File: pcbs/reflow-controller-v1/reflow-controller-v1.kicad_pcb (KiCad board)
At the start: 4 copper layers, 85.2 x 238.5 mm, 154 parts, among them J1 PinHeader 1x03 P2.54mm, J101 EB163A-03-C-180, J102 EB163A-02-C-180, J103 EB163A-02-C-180, J104 EB163A-02-C-180, J105 EB163A-02-C-180, J106 PinHeader 1x03 P2.54mm, J1101 EB163A-04-C-180, J1201 EB163A-04-C-180, J1301 EB163A-04-C-180, J201 PinHeader 1x02 P2.54mm, J3 SWD, J4 UART, M101 47053-1000, Q1601 MMBT3904, Q1602 140357145200, Q201 PMV65XP, SW1001 TS04-66-85-BK-160-SMT, SW1002 PEC12R-3220F-S0024, SW1003 TS04-66-85-BK-160-SMT, U1 TMP1075DSG, U1101 MAX31865ATP+, U1201 MAX31865ATP+, U1301 MAX31865ATP+, U2 TMP1075DSG, U201 TPS62933DRLR, U202 AZ1117-3.3, U3 STM32G474VETx, U301 MOC3043SM, U401 MOC3043SM, U501 MOC3043SM, U601 MOC3043SM

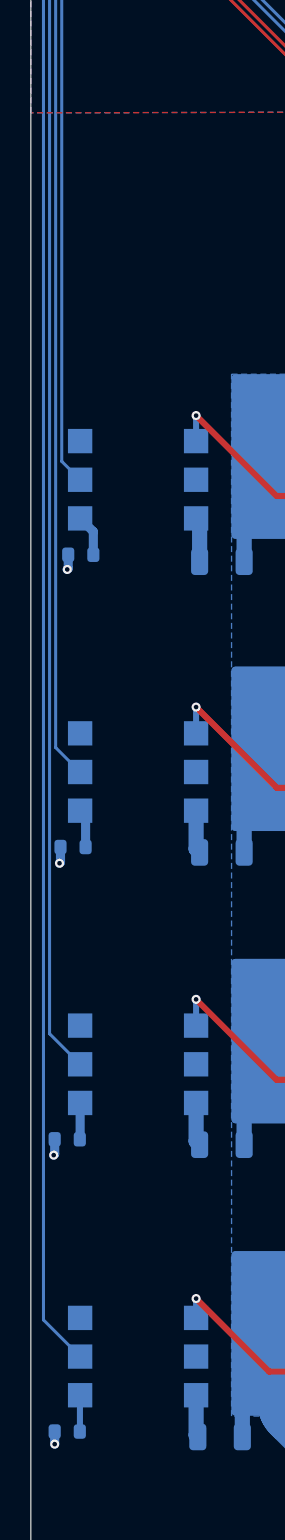
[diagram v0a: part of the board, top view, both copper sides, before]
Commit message: improve powerdelivery to optotriacs
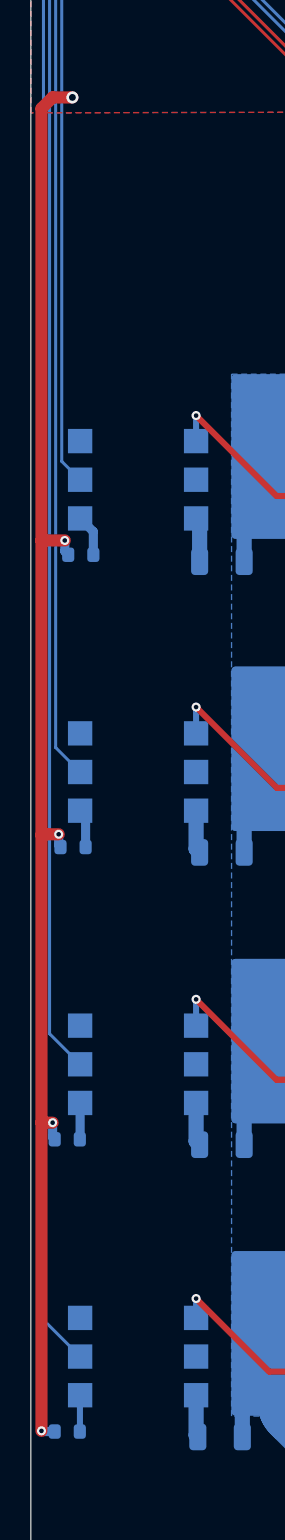
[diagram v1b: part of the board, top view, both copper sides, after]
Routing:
- net +3V3: track 98.0 -> 190.6 mm, vias 32 -> 33
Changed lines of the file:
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@@
 	)
 	(segment
+		(start 17.8308 144.3736)
+		(end 19.134 144.3736)
+		(width 0.8)
+		(layer "F.Cu")
+		(net 2)
+	)
+	(segment
+		(start 17.1026 145.1018)
+		(end 17.8308 144.3736)
+		(width 0.8)
+		(layer "F.Cu")
+		(net 2)
+	)
+	(segment
+		(start 17.1026 192.8368)
+		(end 17.1026 173.482)
+		(width 0.8)
+		(layer "F.Cu")
+		(net 2)
+	)
+	(segment
 		(start 87.2046 85.9692)
 		(end 73.1456 85.9692)
@@
 		(net 2)
 	)
+	(segment
+		(start 17.834 211.7344)
+		(end 17.1026 211.7344)
+		(width 0.8)
+		(layer "F.Cu")
+		(net 2)
+	)
+	(segment
+		(start 17.1026 231.9856)
+		(end 17.1026 211.7344)
+		(width 0.8)
+		(layer "F.Cu")
+		(net 2)
+	)
+	(segment
+		(start 17.1026 173.482)
+		(end 17.1026 145.1018)
+		(width 0.8)
+		(layer "F.Cu")
+		(net 2)
+	)
+	(segment
+		(start 18.234 192.786)
+		(end 17.1534 192.786)
+		(width 0.8)
+		(layer "F.Cu")
+		(net 2)
+	)
+	(segment
+		(start 17.1534 192.786)
+		(end 17.1026 192.8368)
+		(width 0.8)
+		(layer "F.Cu")
+		(net 2)
+	)
+	(segment
+		(start 17.1026 211.7344)
+		(end 17.1026 192.8368)
+		(width 0.8)
+		(layer "F.Cu")
+		(net 2)
+	)
+	(segment
+		(start 18.634 173.482)
+		(end 17.1026 173.482)
+		(width 0.8)
+		(layer "F.Cu")
+		(net 2)
+	)
 	(via
 		(at 54.102 144.78)
@@
 	)
 	(via
-		(at 17.971 232.854)
+		(at 17.1026 231.9856)
 		(size 0.6)
 		(drill 0.3)
@@
 	)
 	(via
-		(at 18.288 194.691)
+		(at 18.234 192.786)
 		(size 0.6)
 		(drill 0.3)
@@
 	)
 	(via
-		(at 17.907 213.868)
+		(at 17.834 211.7344)
 		(size 0.6)
 		(drill 0.3)
@@
 	)
 	(via
-		(at 18.796 175.387)
+		(at 18.634 173.482)
 		(size 0.6)
 		(drill 0.3)
@@
 	)
 	(via
+		(at 19.134 144.3736)
+		(size 0.8)
+		(drill 0.45)
+		(layers "F.Cu" "B.Cu")
+		(free yes)
+		(net 2)
+	)
+	(via
 		(at 49.4792 74.1934)
 		(size 0.6)
@@
 	)
 	(segment
+		(start 18.634 174.1958)
+		(end 18.86 174.4218)
+		(width 0.6)
+		(layer "B.Cu")
+		(net 2)
+	)
+	(segment
 		(start 54.102 152.576)
 		(end 54.102 144.78)
@@
 	)
 	(segment
-		(start 18.352 194.627)
-		(end 18.288 194.691)
-		(width 0.6)
-		(layer "B.Cu")
-		(net 2)
-	)
-	(segment
 		(start 70.4088 88.5444)
 		(end 70.5704 88.5444)
@@
 	)
 	(segment
-		(start 18.86 175.323)
-		(end 18.796 175.387)
-		(width 0.6)
-		(layer "B.Cu")
-		(net 2)
-	)
-	(segment
 		(start 74.9282 108.9232)
 		(end 74.9282 110.3988)
@@
 	)
 	(segment
+		(start 17.1026 231.9856)
+		(end 17.146 232.029)
+		(width 0.6)
+		(layer "B.Cu")
+		(net 2)
+	)
+	(segment
 		(start 28.9182 70.9298)
 		(end 28.9052 70.9168)
@@
 	)
 	(segment
+		(start 17.146 232.029)
+		(end 17.971 232.029)
+		(width 0.6)
+		(layer "B.Cu")
+		(net 2)
+	)
+	(segment
 		(start 76.9112 89.4662)
 		(end 74.5744 89.4662)
@@
 	)
 	(segment
-		(start 17.971 212.8266)
-		(end 17.971 213.804)
+		(start 17.834 212.6896)
+		(end 17.971 212.8266)
 		(width 0.6)
 		(layer "B.Cu")
@@
 	)
 	(segment
-		(start 18.86 174.4218)
-		(end 18.86 175.323)
-		(width 0.6)
-		(layer "B.Cu")
-		(net 2)
-	)
-	(segment
 		(start 31.585 76.811)
 		(end 29.525 76.811)
@@
 	)
 	(segment
+		(start 18.234 193.5062)
+		(end 18.352 193.6242)
+		(width 0.6)
+		(layer "B.Cu")
+		(net 2)
+	)
+	(segment
 		(start 44.982 91.9895)
 		(end 44.982 92.813)
@@
 	)
 	(segment
-		(start 17.971 232.854)
-		(end 17.971 232.029)
-		(width 0.6)
-		(layer "B.Cu")
-		(net 2)
-	)
-	(segment
 		(start 82.369 58.5816)
 		(end 82.55 58.7626)
@@
 	)
 	(segment
-		(start 17.971 213.804)
-		(end 17.907 213.868)
-		(width 0.6)
-		(layer "B.Cu")
-		(net 2)
-	)
-	(segment
 		(start 75.375 111.4552)
 		(end 76.2386 112.3188)
@@
 	)
 	(segment
-		(start 18.352 193.6242)
-		(end 18.352 194.627)
+		(start 18.234 192.786)
+		(end 18.234 193.5062)
+		(width 0.6)
+		(layer "B.Cu")
+		(net 2)
+	)
+	(segment
+		(start 18.634 173.482)
+		(end 18.634 174.1958)
 		(width 0.6)
 		(layer "B.Cu")
@@
 	)
 	(segment
+		(start 17.834 211.7344)
+		(end 17.834 212.6896)
+		(width 0.6)
+		(layer "B.Cu")
+		(net 2)
+	)
+	(segment
 		(start 75.375 110.8456)
 		(end 75.375 111.4552)
@@
 		(polygon
 			(pts
-				(xy 16.383 15.24) (xy 101.5238 15.24) (xy 101.5746 159.6644) (xy 64.516 159.7152) (xy 64.516015 145.209658)
-				(xy 20.49774 145.237321) (xy 20.5486 233.299) (xy 16.4084 233.2736)
+				(xy 16.383 15.24) (xy 101.5238 15.24) (xy 101.5746 159.6644) (xy 64.516 159.7152) (xy 64.516015 145.288)
+				(xy 16.4084 145.3896)
 			)
 		)

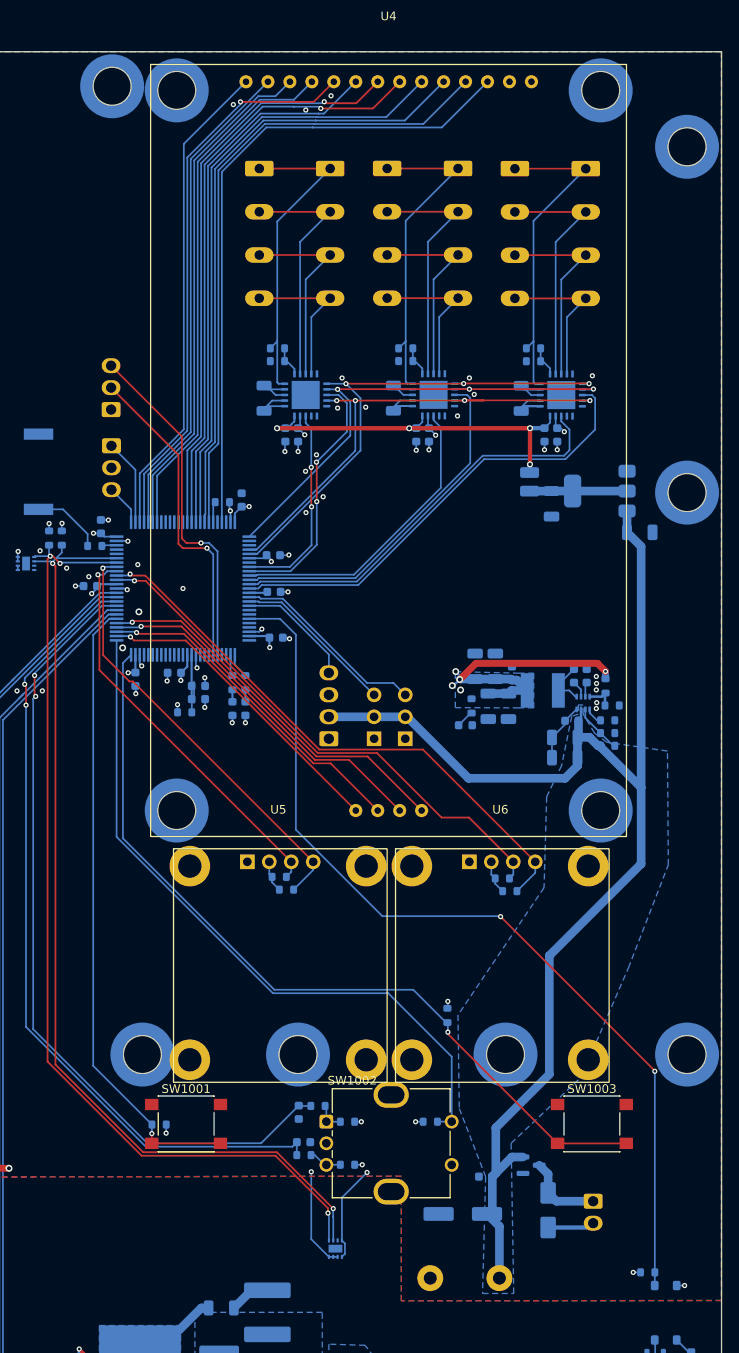
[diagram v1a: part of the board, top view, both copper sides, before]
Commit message: add clear border between HV&LV
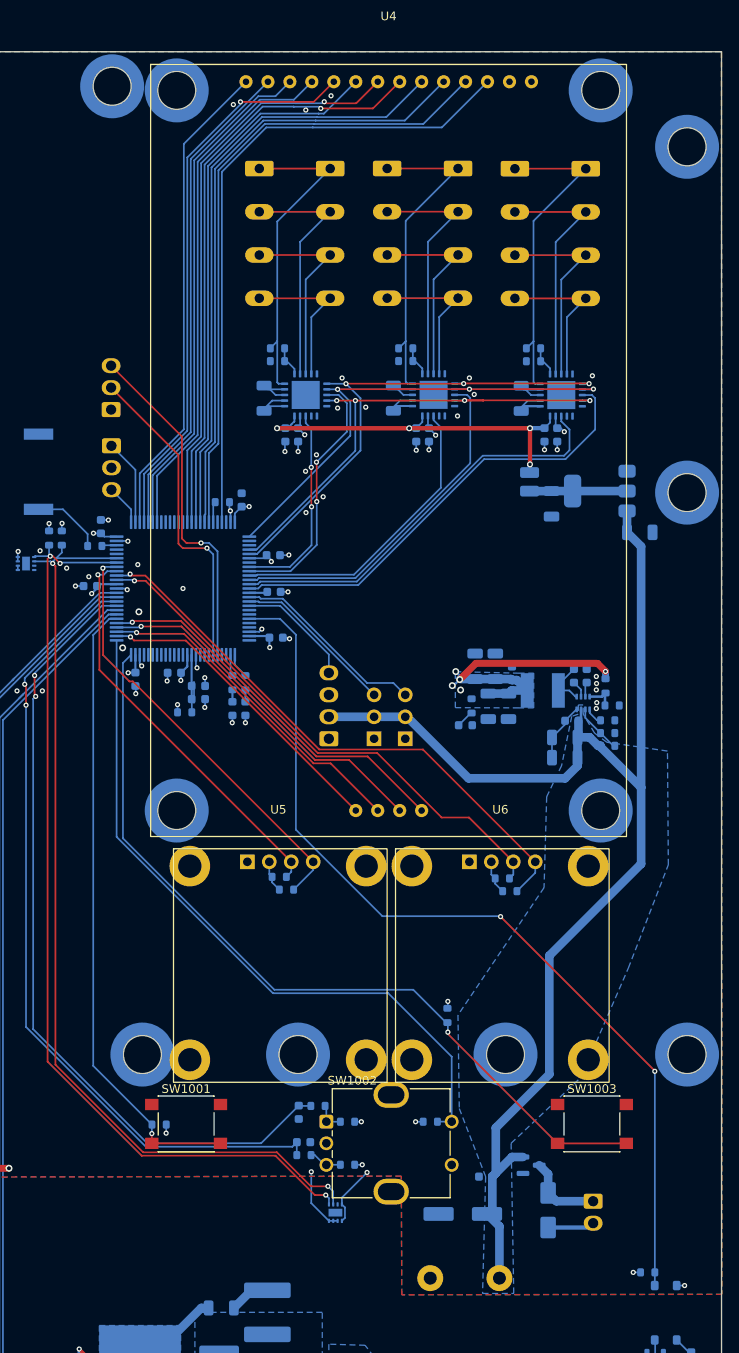
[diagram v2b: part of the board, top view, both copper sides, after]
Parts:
- moved U2 4.17 mm to (56.9, 149.5)
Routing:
- net +3V3: track 190.6 -> 186.4 mm
- net GND: track 48.7 -> 44.5 mm
- net /Temperature onboard 1/SDA: track 113.1 -> 109.7 mm
- net /Temperature onboard 1/SCL: track 112.8 -> 109.8 mm

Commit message: update pcb size&display positioning
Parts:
- moved R2 119.2 mm to (120.8, 142.7), turned to 180 degrees
- moved R1 118.9 mm to (120.8, 140.2), turned to 180 degrees
- moved U1 116.3 mm to (116.6, 140.8)
- moved Q1602 99.2 mm to (31.9, 237.5), turned to 180 degrees
- moved R1603 93.9 mm to (37.2, 237.9), turned to 0 degrees
- moved R1605 92.9 mm to (59.8, 69.7), turned to 90 degrees
- moved Q1601 92.9 mm to (37.5, 240.7)
- moved D1601 92.2 mm to (42.4, 250.8)
- moved D1603 92.2 mm to (37.7, 250.8)
- moved D1604 92.2 mm to (40.1, 250.8)
- moved R1604 92.2 mm to (38.1, 247.8)
- moved D1602 92.2 mm to (41.1, 254.2)
- moved D1605 92.0 mm to (38.1, 244.9)
- moved C1602 90.9 mm to (41.6, 243.7), turned to -90 degrees
- moved R1601 80.6 mm to (45.2, 240.8), turned to -90 degrees
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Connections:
- J4 pad 2: /microcontroller/USART1_RX -> /microcontroller/USART2_RX
- J4 pad 3: /microcontroller/USART1_TX -> /microcontroller/USART2_TX
- U3 pad 15: /Servo1 -> unconnected-(U3-PC0-Pad15)
- U3 pad 16: /Servo2 -> unconnected-(U3-PC1-Pad16)
- U3 pad 17: /Fan_PWM -> unconnected-(U3-PC2-Pad17)
- U3 pad 30: /microcontroller/USART1_TX -> unconnected-(U3-PC4-Pad30)
- U3 pad 31: /microcontroller/USART1_RX -> unconnected-(U3-PC5-Pad31)
- U3 pad 39: unconnected-(U3-PE8-Pad39) -> /Servo1
- U3 pad 40: unconnected-(U3-PE9-Pad40) -> /Servo2
- U3 pad 42: unconnected-(U3-PE11-Pad42) -> /Fan_PWM
- U3 pad 87: unconnected-(U3-PD5-Pad87) -> /microcontroller/USART2_TX
- U3 pad 88: unconnected-(U3-PD6-Pad88) -> /microcontroller/USART2_RX
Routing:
- net /Temperature onboard 1/SCL: track 109.8 -> 0.00 mm, vias 2 -> 0
- net /Temperature onboard 1/SDA: track 109.7 -> 0.00 mm, vias 3 -> 0
- net +3V3: track 186.4 -> 80.7 mm, vias 33 -> 23
- net /Phase_L: track 111.9 -> 28.2 mm, vias 16 -> 12
- net /Buttons/SW_Encoder: track 81.2 -> 0.00 mm
- net /Zero Crossing detector/Crossing: track 106.6 -> 182.8 mm
- net /Buttons/SW_2: track 95.2 -> 27.2 mm
- net /Buttons/SW_1: track 73.1 -> 10.1 mm
- net /Display OLED 2/I2C_SDA: track 66.6 -> 4.57 mm, vias 1 -> 0
- net /Display OLED 2/I2C_SCL: track 61.5 -> 5.88 mm
- net /Buttons/Encoder_A: track 93.5 -> 39.5 mm, vias 2 -> 1
- net /Buttons/Encoder_B: track 93.5 -> 43.2 mm, vias 2 -> 1
- net /microcontroller/USART1_TX: track 40.1 -> 0.00 mm, vias 1 -> 0
- net /microcontroller/USART1_RX: track 37.4 -> 0.00 mm, vias 1 -> 0
- net /Display LCD/Touch: track 44.5 -> 18.0 mm
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- removed copper zone on F.Cu, net /Phase_L
- removed copper zone on B.Cu, net /Phase_N
- removed copper zone on B.Cu, net /SSR 1/MAIN_OUT
- removed copper zone on B.Cu, net /SSR 2/MAIN_OUT
- removed copper zone on B.Cu, net /SSR 3/MAIN_OUT
- removed copper zone on B.Cu, net /SSR 4/MAIN_OUT
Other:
- board size 85.2 x 238.5 mm -> 74.9 x 243.5 mm
- board text added: "Fix it"
- board text added: "Standofs NEED to be at least 23mm to clear the DCDC module"

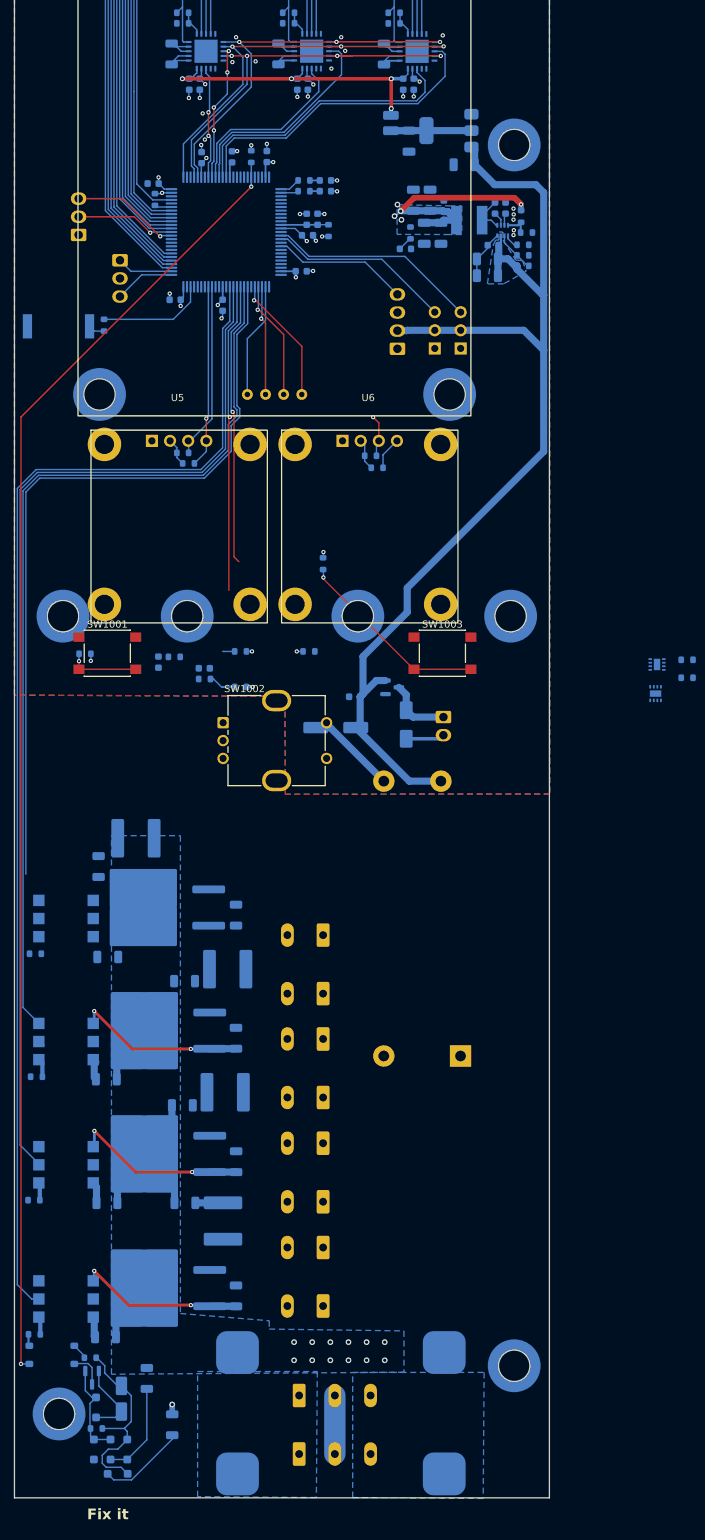
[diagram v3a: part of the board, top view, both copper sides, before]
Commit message: update hv placment&routing + add initiall hv lv seperation
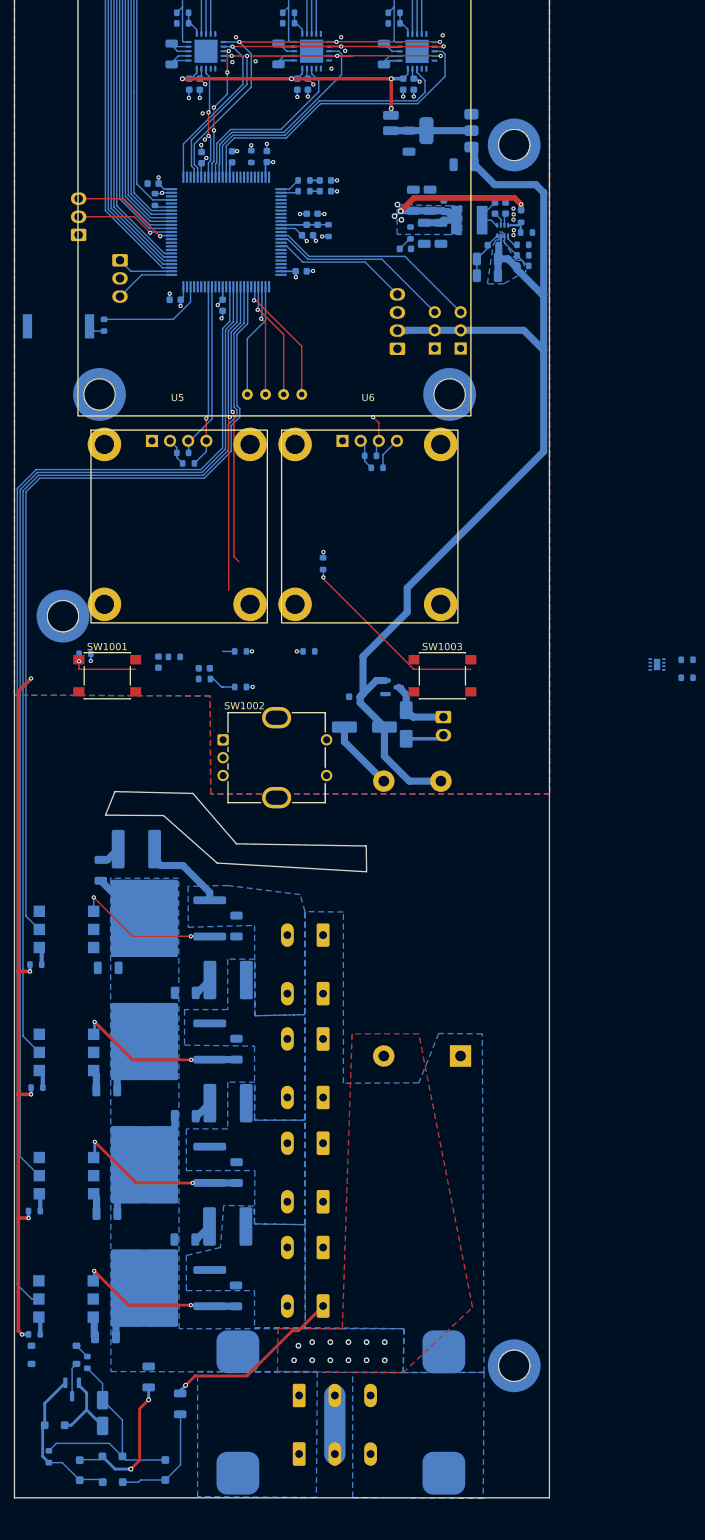
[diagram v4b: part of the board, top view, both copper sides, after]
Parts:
- removed H4, H5, H6, H7: MountingHole_Pad, Mounting_Wuerth:Mounting_Wuerth_WA-SMSI-M3_H15mm_9774150360
- removed U2: TMP1075DSG, Package_SON:WSON-8-1EP_2x2mm_P0.5mm_EP0.9x1.6mm
- moved H9 111.8 mm to (33.4, 134.0)
- moved R1604 7.75 mm to (31.4, 251.8), turned to -90 degrees
- moved D1602 6.70 mm to (47.8, 253.6), turned to -90 degrees
- moved D1605 6.30 mm to (32.3, 247.4), turned to 0 degrees
- moved D1603 5.28 mm to (40.4, 255.3), turned to 180 degrees
- moved D1604 5.20 mm to (35.8, 253.7), turned to -90 degrees
- moved R604 5.13 mm to (50.5, 221.4)
- moved C202 4.02 mm to (75.6, 149.6)
- moved C1602 3.32 mm to (39.0, 245.7)
- moved Q1601 3.25 mm to (34.7, 242.4)
- moved SW1001 3.15 mm to (39.6, 142.4)
- moved SW1003 3.15 mm to (86.6, 142.4)
- moved R1602 3.14 mm to (49.8, 244.4)
- moved SW1002 2.39 mm to (55.8, 151.4)
- moved D1601 2.30 mm to (40.3, 251.7), turned to 180 degrees
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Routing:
- net /Zero Crossing detector/Crossing: track 182.8 -> 0.00 mm, vias 2 -> 0
- net +3V3: track 80.7 -> 180.6 mm, vias 23 -> 28
- net /Phase_N: track 1.37 -> 25.3 mm
- net Net-(D301-G): track 0.00 -> 20.5 mm, vias 0 -> 2
- net /SSR 1/MAIN_OUT: track 0.00 -> 12.2 mm
- net /SSR 1/IN: track 109.0 -> 117.5 mm
- net Net-(D1603-A): track 13.5 -> 21.6 mm
- net Net-(D1601-A): track 13.4 -> 20.6 mm, vias 0 -> 2
- net Net-(D1601-K): track 27.2 -> 32.1 mm
- net /SSR 2/IN: track 131.5 -> 135.4 mm
- net Net-(D1602-A): track 12.3 -> 16.2 mm
- net Net-(C301-Pad1): track 0.00 -> 3.06 mm
- net GND: track 42.5 -> 39.7 mm
- net Net-(C501-Pad1): track 0.00 -> 2.74 mm
- net Net-(C401-Pad1): track 0.00 -> 2.74 mm
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- added copper zone on F.Cu, net /Phase_L
- added copper zone on B.Cu, net /Phase_N
- added copper zone on B.Cu, net /SSR 1/MAIN_OUT
- added copper zone on B.Cu, net /SSR 2/MAIN_OUT
- added copper zone on B.Cu, net /SSR 3/MAIN_OUT
- added copper zone on B.Cu, net /SSR 4/MAIN_OUT
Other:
- outline, holes or cut-outs redrawn
- board text removed: "Fix it"

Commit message: update display placing & prelim. routing
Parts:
- U1: footprint Package_SON:WSON-8-1EP_2x2mm_P0.5mm_EP0.9x1.6mm -> Package_SON:WSON-8-1EP_2x2mm_P0.5mm_EP0.9x1.6mm_ThermalVias
- moved R1 62.8 mm to (59.7, 154.6), turned to 0 degrees
- moved R2 59.4 mm to (62.7, 154.6)
- moved U1 58.1 mm to (60.8, 157.0), turned to -90 degrees
- moved H9 17.4 mm to (50.8, 134.0)
- moved R1009 16.2 mm to (81.7, 137.8), turned to 180 degrees
- moved R1007 14.2 mm to (69.5, 153.1)
- moved R1005 13.4 mm to (58.1, 149.7), turned to 0 degrees
- moved R1004 12.5 mm to (58.1, 156.4)
- moved C1002 12.4 mm to (57.5, 146.6), turned to 180 degrees
- moved R1006 12.1 mm to (57.5, 154.2), turned to 90 degrees
- moved C1001 11.7 mm to (58.2, 152.0)
- moved R1003 10.2 mm to (55.8, 148.9), turned to -90 degrees
- moved M101 8.86 mm to (74.8, 103.6)
- moved J1 8.86 mm to (80.1, 103.6)
- moved J106 8.82 mm to (83.8, 103.6)
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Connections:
- H1 pad 1: Net-(H1-Pad1) -> unconnected-(H1-Pad1)_1
- H2 pad 1: Net-(H1-Pad1) -> unconnected-(H2-Pad1)_2
- H3 pad 1: Net-(H1-Pad1) -> unconnected-(H3-Pad1)_3
- H8 pad 1: Net-(H1-Pad1) -> unconnected-(H8-Pad1)_2
- H9 pad 1: Net-(H1-Pad1) -> unconnected-(H9-Pad1)_3
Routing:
- net /Zero Crossing detector/Crossing: track 0.00 -> 182.5 mm, vias 0 -> 2
- net /Temperature onboard 1/SCL: track 0.00 -> 72.9 mm, vias 0 -> 2
- net /Temperature onboard 1/SDA: track 0.00 -> 71.9 mm, vias 0 -> 2
- net /Buttons/SW_Encoder: track 0.00 -> 68.5 mm
- net /Buttons/SW_1: track 10.1 -> 75.6 mm
- net /Buttons/SW_2: track 27.2 -> 74.1 mm
- net /Display OLED 2/I2C_SDA: track 4.57 -> 45.5 mm, vias 0 -> 1
- net /Display OLED 2/I2C_SCL: track 5.88 -> 38.9 mm
- net /Buttons/Encoder_A: track 39.5 -> 62.6 mm, vias 1 -> 2
- net /Buttons/Encoder_B: track 43.2 -> 65.9 mm, vias 1 -> 2
- net /SSR 1/IN: track 117.5 -> 107.7 mm
- net /SSR 2/IN: track 135.4 -> 125.6 mm
- net /SSR 3/IN: track 151.5 -> 142.1 mm
- net /SSR 4/IN: track 169.6 -> 160.2 mm
- net +3V3: track 180.6 -> 189.7 mm, vias 28 -> 30
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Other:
- board text added: "TODO: - Plane/Via Stitching"
- board text removed: "TODO: - Find fitting mounting for display - Connect earth to Digital ground? - Correct display mounting - Ground/eath mounting holes? - Plane/Via Stitching"
